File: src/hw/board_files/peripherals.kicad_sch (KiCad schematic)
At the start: 27 parts, among them J7 Conn_01x04, J8 Molex 104031-0811, Q1 PMOS, U5 NEO-M9N, U7 SHT30-DIS, U8 BQ27411DRZT-G1A

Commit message: Nearly done with layout
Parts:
- D6: footprint Package_TO_SOT_SMD:SOT-23-3 -> Package_TO_SOT_SMD:SOT-23_Handsoldering
- Q1: footprint Library:SOT91P240X110-3N_DMG2305UX-7 -> Package_TO_SOT_SMD:SOT-23_Handsoldering
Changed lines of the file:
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@@
 			)
 		)
-		(property "Footprint" "Package_TO_SOT_SMD:SOT-23-3"
+		(property "Footprint" "Package_TO_SOT_SMD:SOT-23_Handsoldering"
 			(at 233.68 73.66 0)
 			(effects
@@
 			)
 		)
-		(property "Footprint" "Library:SOT91P240X110-3N_DMG2305UX-7"
+		(property "Footprint" "Package_TO_SOT_SMD:SOT-23_Handsoldering"
 			(at 38.1 53.34 0)
 			(effects

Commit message: Updated BOM
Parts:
- R19: renamed from R22; footprint Resistor_SMD:R_0603_1608Metric_Pad0.98x0.95mm_HandSolder -> Resistor_SMD:R_1206_3216Metric_Pad1.30x1.75mm_HandSolder
- renumbered C18 to C17, C19 to C18, C20 to C19, C21 to C20, C22 to C21, D7 to D6, D6 to D7, J7 to J5, J8 to J6, R16 to R14, R17 to R15, R18 to R16, R19 to R17, R21 to R18, R24 to R20, R23 to R21, R20 to R22, TP10 to TP8, TP12 to TP9, U5 to U4, U7 to U5, U8 to U6
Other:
- note added: "Sense resistor (R19) 1% tolerance 1W rating"
- note removed: "Sense resistor (R22) 1% tolerance 1W rating"

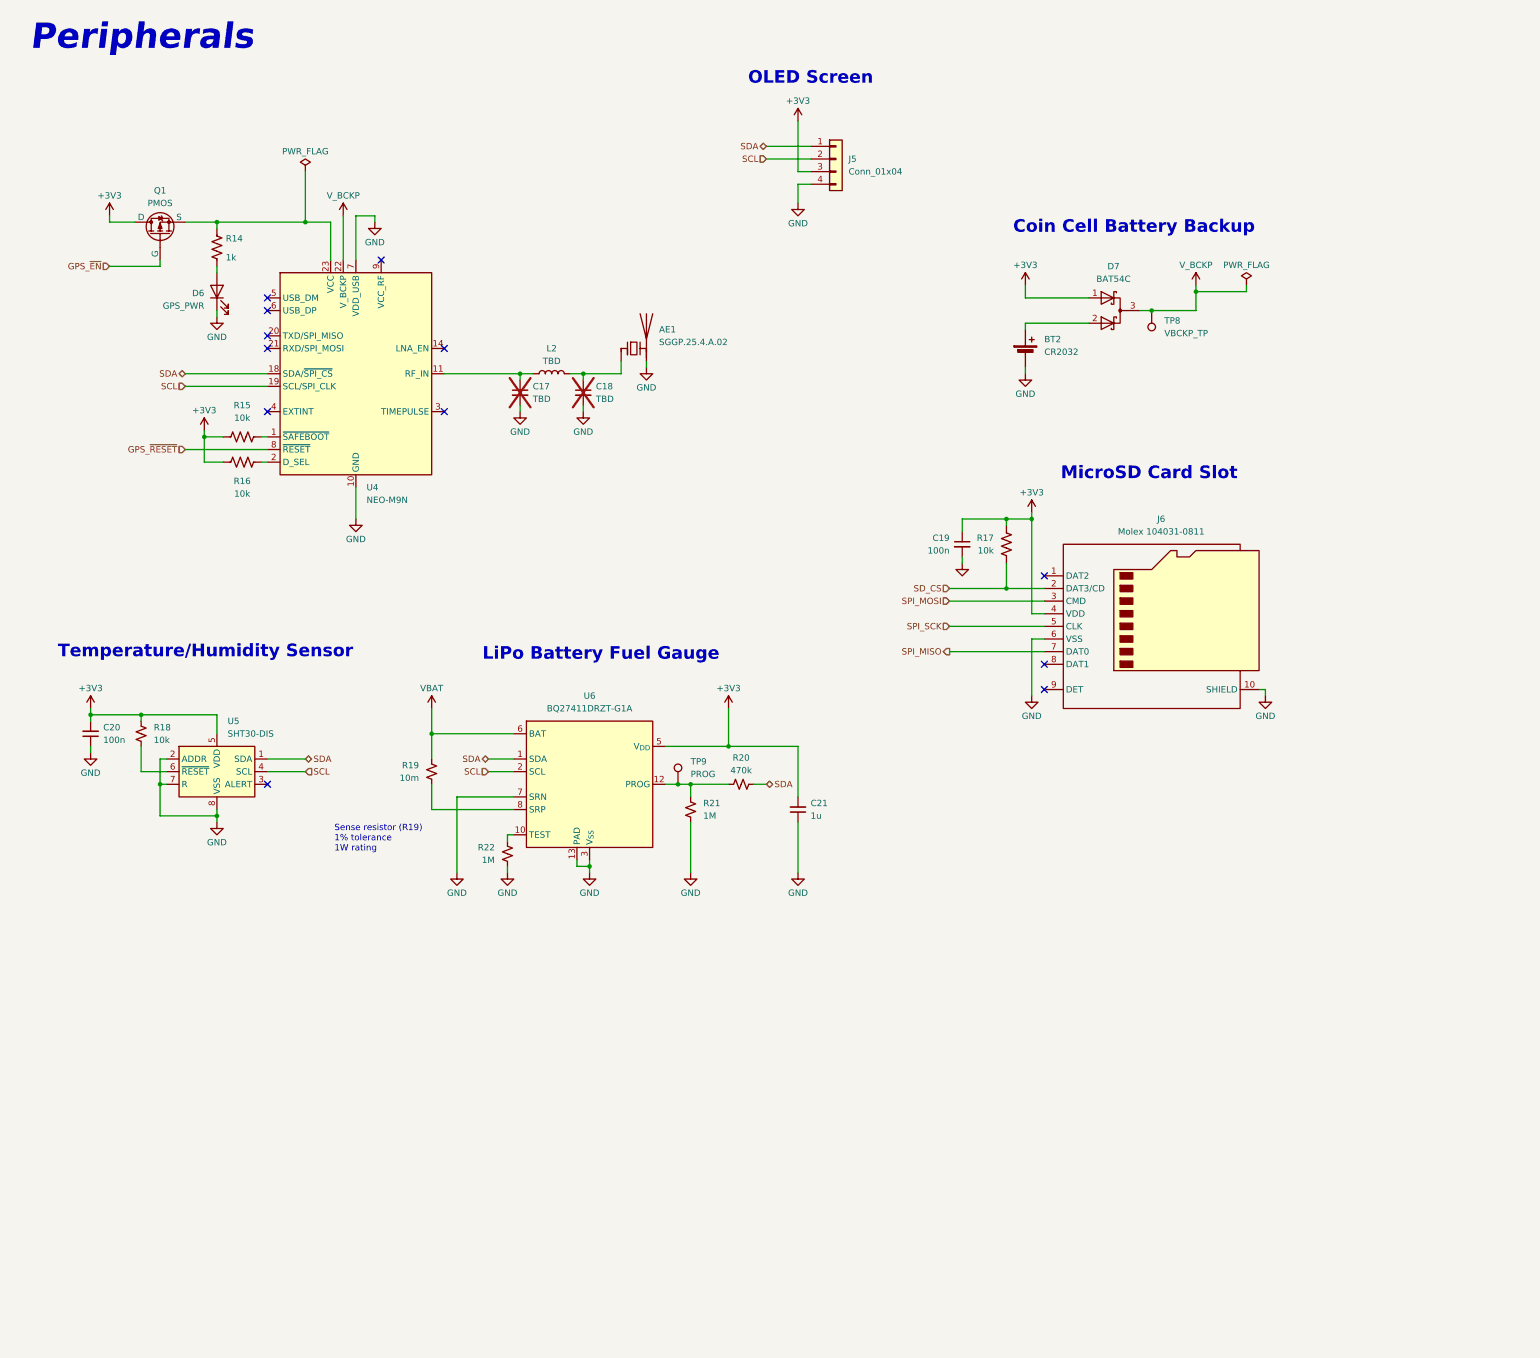
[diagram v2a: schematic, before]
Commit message: Schematic updates
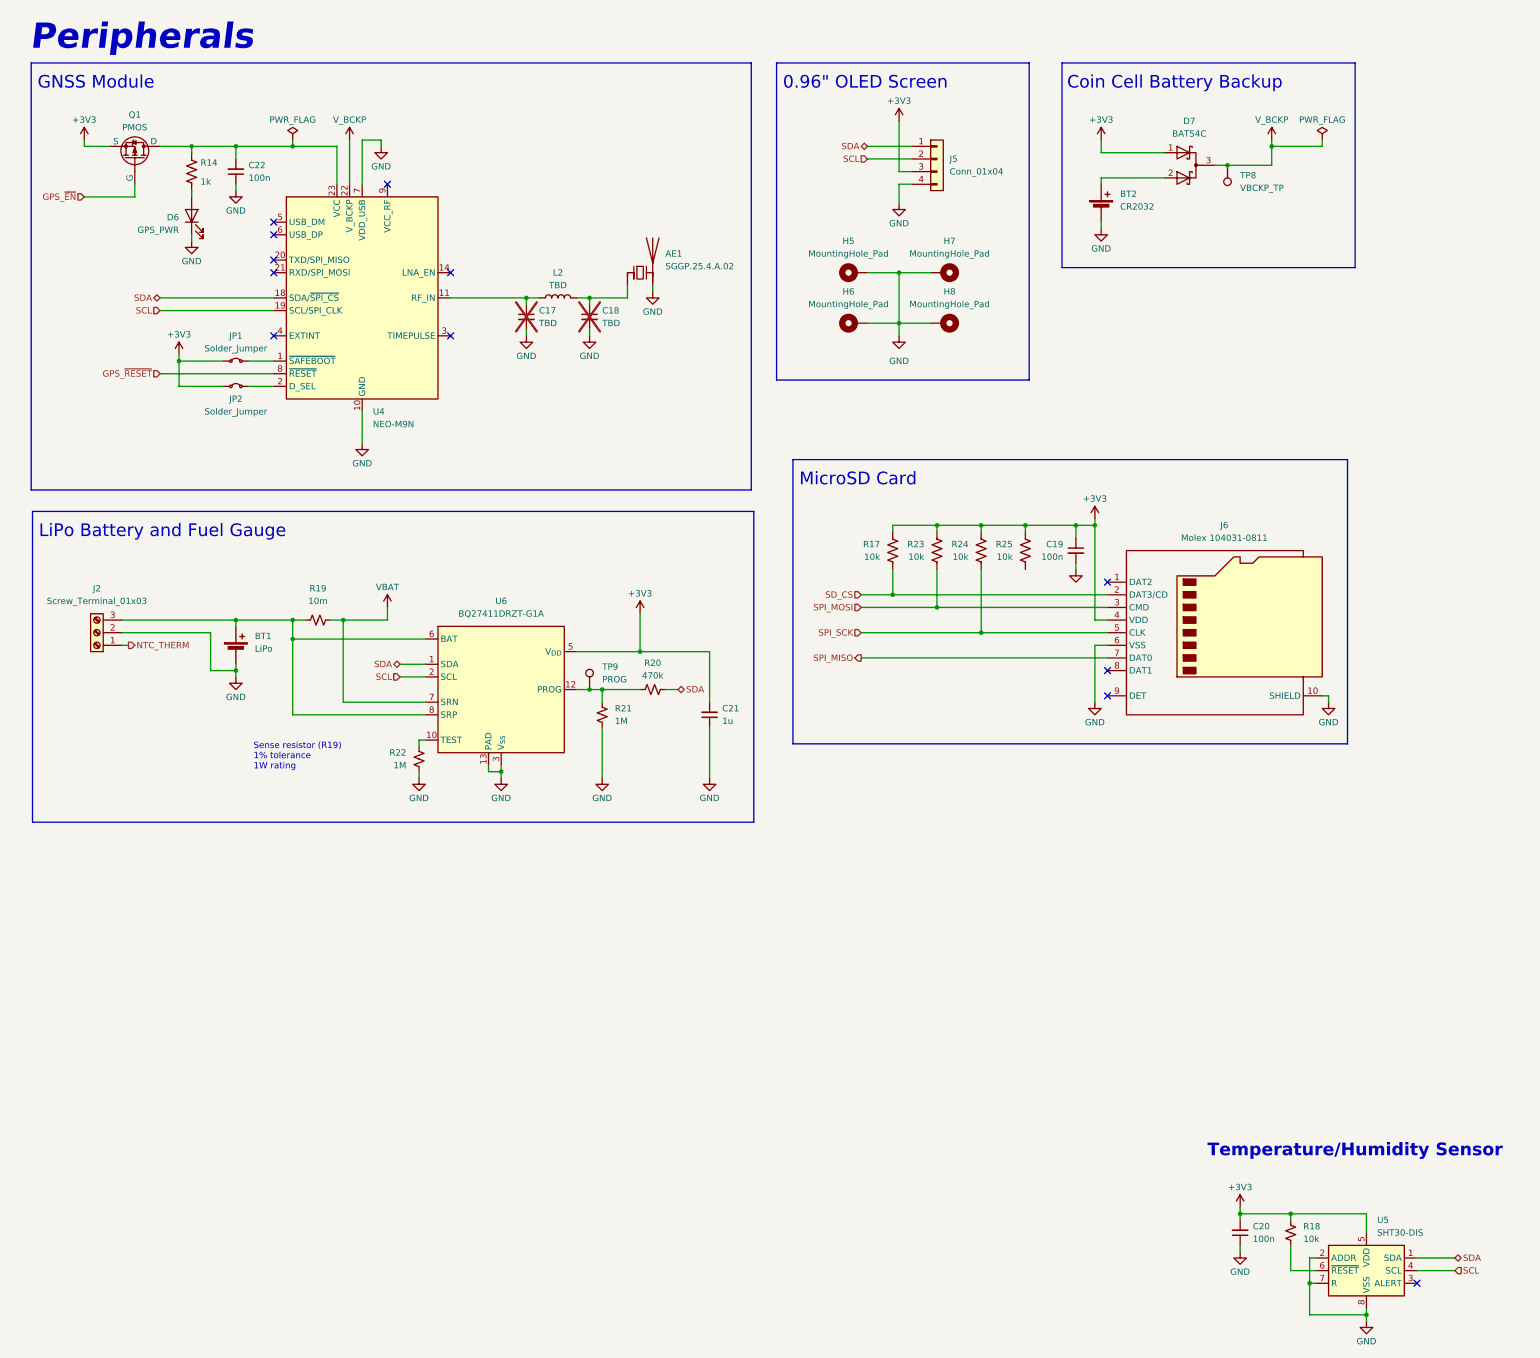
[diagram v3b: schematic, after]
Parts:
- removed R15, R16: 10k, Resistor_SMD:R_0603_1608Metric_Pad0.98x0.95mm_HandSolder, symbol Device:R_US
- added BT1: LiPo, Connector_JST:JST_PH_S2B-PH-K_1x02_P2.00mm_Horizontal, symbol Device:Battery_Cell
- added C22: 100n, Capacitor_SMD:C_0603_1608Metric_Pad1.08x0.95mm_HandSolder, symbol Device:C_Small
- added H5, H6, H7, H8: MountingHole_Pad, symbol Mechanical:MountingHole_Pad
- added J2: Screw_Terminal_01x03, TerminalBlock_Phoenix:TerminalBlock_Phoenix_MPT-0,5-3-2.54_1x03_P2.54mm_Horizontal, symbol Connector:Screw_Terminal_01x03
- added JP1, JP2: Solder_Jumper, Jumper:SolderJumper-2_P1.3mm_Open_TrianglePad1.0x1.5mm, symbol Jumper:Jumper_2_Small_Bridged
- added R23, R24, R25: 10k, Resistor_SMD:R_0603_1608Metric_Pad0.98x0.95mm_HandSolder, symbol Device:R_US
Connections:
- net +3V3: now also Q1.3 (S), JP1.1 (A), JP2.1 (A), R23.1, R24.1, R25.1; no longer Q1.1 (D)
- net GND: now also BT1.2 (-), C22.1, H5.1, H6.1, H7.1, H8.1, J2.2 (Pin_2); no longer U6.7 (SRN)
- net SPI_MOSI: now also R23.2
- net SPI_SCK: now also R24.2
- net VBAT: now also R19.2, U6.7 (SRN); no longer R19.1, U6.6 (BAT)
- net at U6.8 (SRP): now also R19.1, U6.6 (BAT), BT1.1 (+), J2.3 (Pin_3); no longer R19.2
- net at U4.1 (~{SAFEBOOT}): now also JP1.2 (B)
- net at U4.2 (D_SEL): now also JP2.2 (B)
- net at R14.1, U4.23 (VCC): now also Q1.1 (D), C22.2; no longer Q1.3 (S)
- new net NTC_THERM: J2.1 (Pin_1)
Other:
- note added: "0.96" OLED Screen"
- note added: "GNSS Module"
- note added: "LiPo Battery and Fuel Gauge"
- note added: "MicroSD Card"
- note removed: "LiPo Battery Fuel Gauge"
- note removed: "MicroSD Card Slot"
- note removed: "OLED Screen"
- moved on the sheet: AE1, BT2, C17, C18, C19, C20, C21, D6, D7, J5, J6, L2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

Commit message: Fixed fuel gauge IC schematic
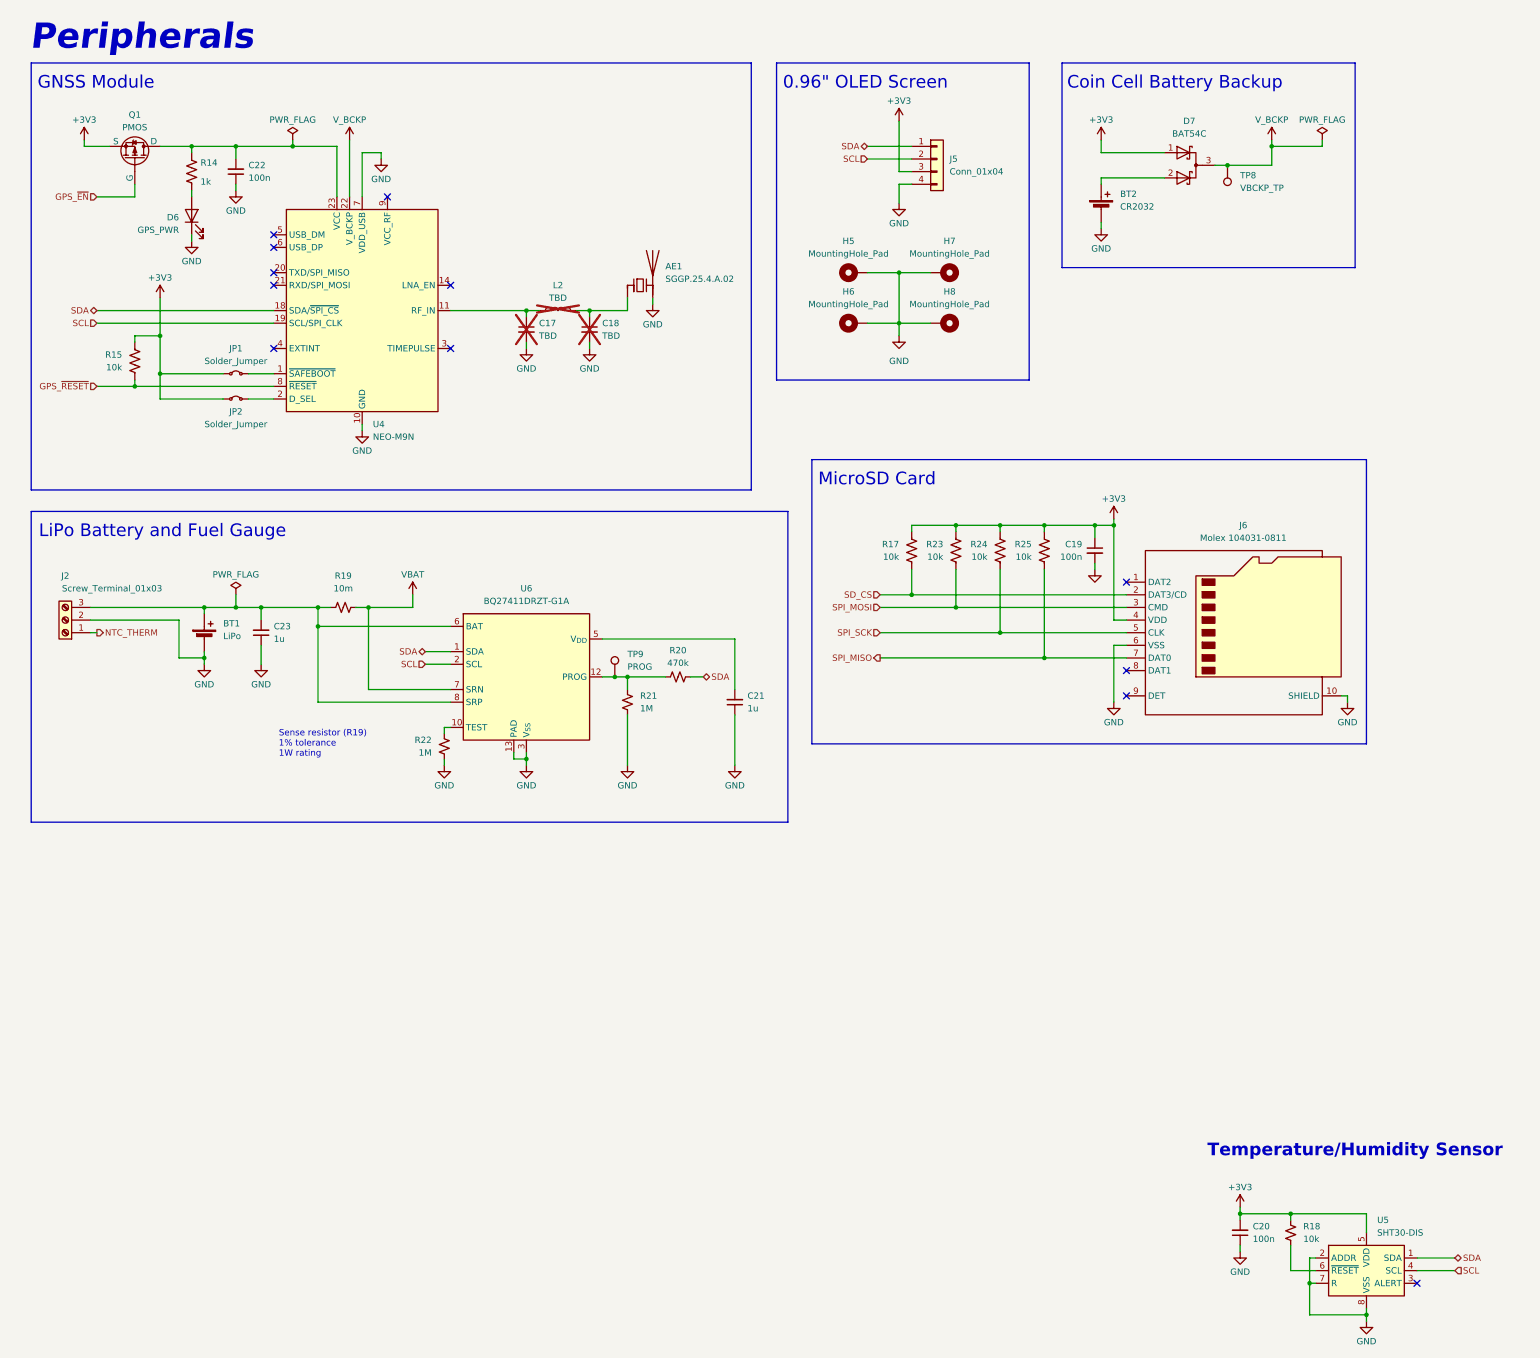
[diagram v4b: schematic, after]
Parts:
- added C23: 1u, Capacitor_SMD:C_0603_1608Metric_Pad1.08x0.95mm_HandSolder, symbol Device:C_Small
- added R15: 10k, Resistor_SMD:R_0603_1608Metric_Pad0.98x0.95mm_HandSolder, symbol Device:R_US
- L2: now not fitted; now left out of the parts list
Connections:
- net +3V3: now also R15.1; no longer C21.2, U6.5 (V_{DD})
- net GND: now also C23.1
- net GPS_~{RESET}: now also R15.2
- net SPI_MISO: now also R25.2
- net at BT1.1 (+), J2.3 (Pin_3), R19.1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: now also C23.2
- new net: C21.2, U6.5 (V_{DD})
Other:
- moved on the sheet: AE1, BT1, C17, C18, C19, C21, J2, J6, JP1, JP2, R17, R19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

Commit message: Added new OLED footprint. Finished schematic updates, started lyout. Changed 10 mOhm sense resistor PN to TCR of 50 ppm/C
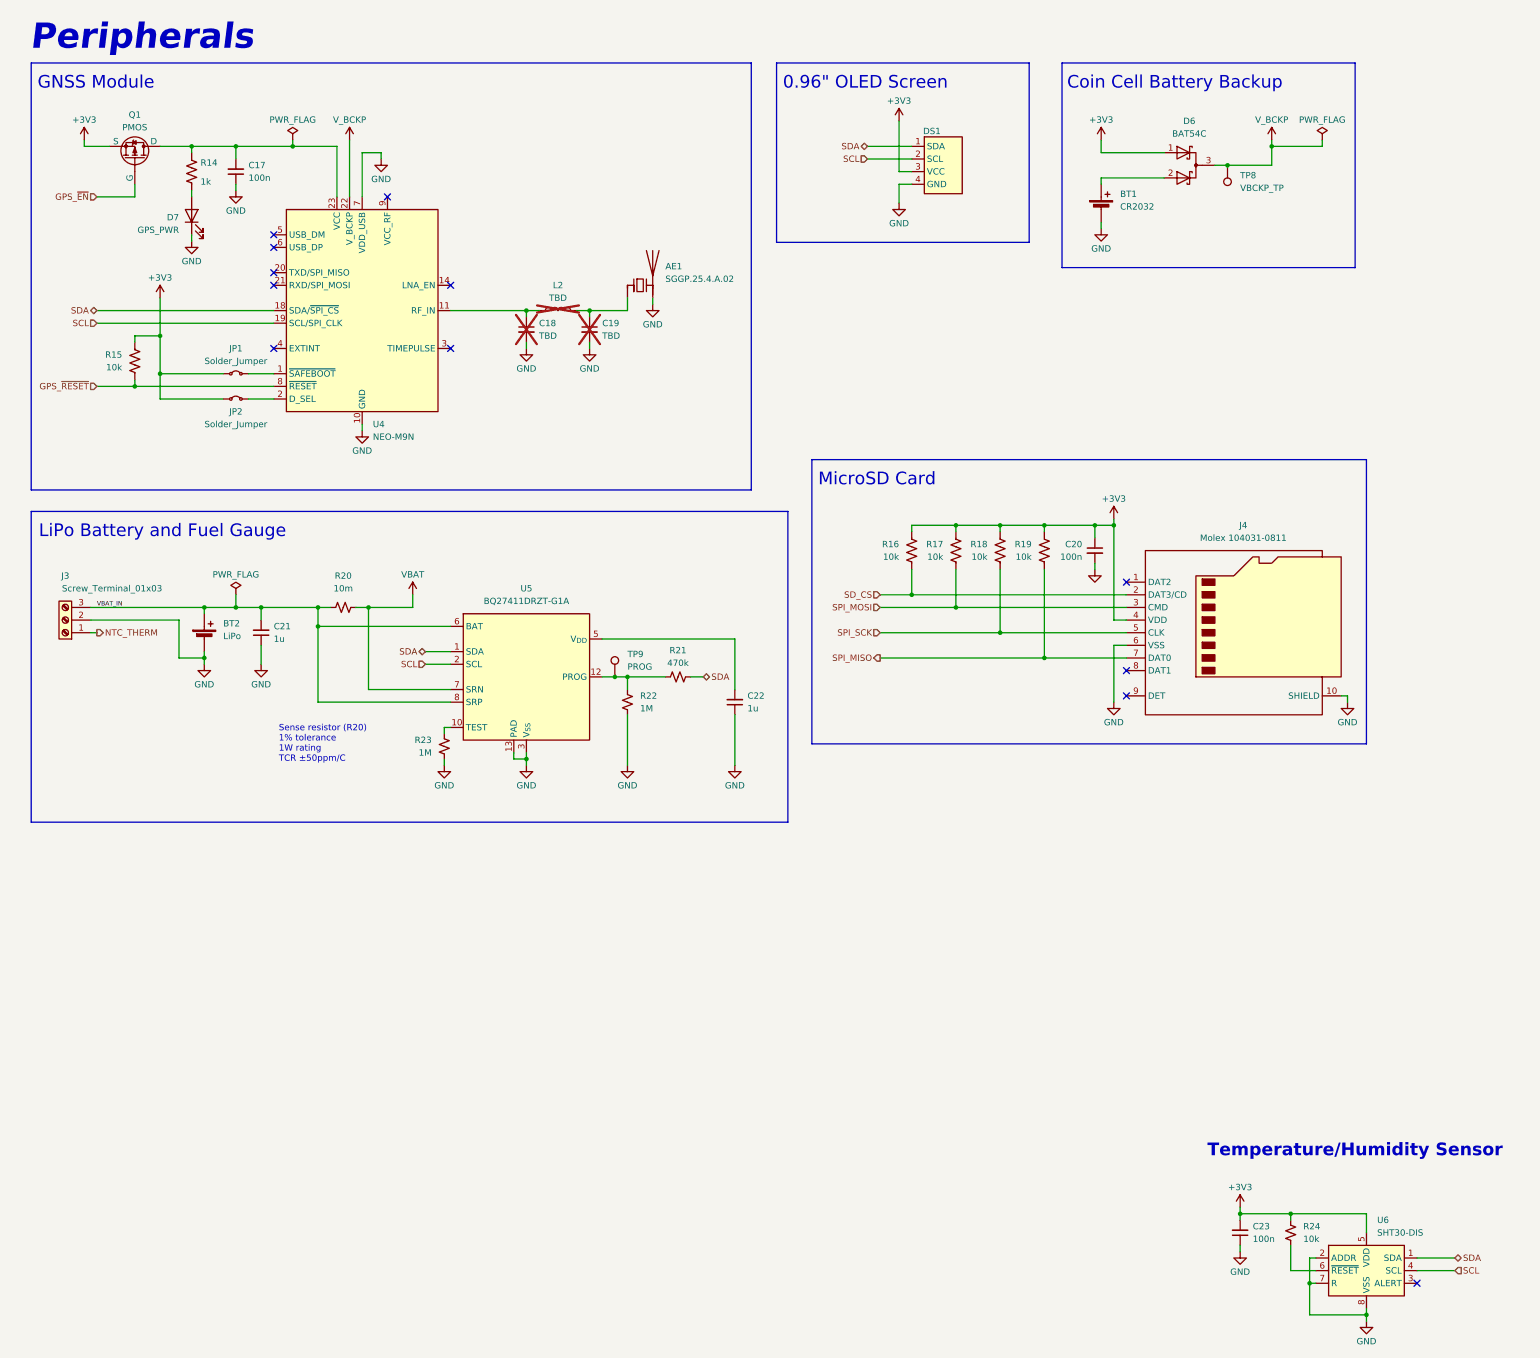
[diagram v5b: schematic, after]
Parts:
- removed H5, H6, H7, H8: MountingHole_Pad, symbol Mechanical:MountingHole_Pad
- removed J5: Conn_01x04, Connector_PinSocket_2.54mm:PinSocket_1x04_P2.54mm_Vertical, symbol Connector_Generic:Conn_01x04
- added DS1: ~, Project_Library:OLED_128x64_0.96in, symbol Project_Library:OLED_128x64
- J3: renamed from J2; footprint TerminalBlock_Phoenix:TerminalBlock_Phoenix_MPT-0,5-3-2.54_1x03_P2.54mm_Horizontal -> TerminalBlock_TE-Connectivity:TerminalBlock_TE_282834-3_1x03_P2.54mm_Horizontal
- renumbered BT2 to BT1, BT1 to BT2, C22 to C17, C17 to C18, C18 to C19, C19 to C20, C23 to C21, C21 to C22, C20 to C23, D7 to D6, D6 to D7, J6 to J4, R17 to R16, R23 to R17, R24 to R18, R25 to R19, R19 to R20, R20 to R21, R21 to R22, R22 to R23, R18 to R24, U6 to U5, U5 to U6
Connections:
- net +3V3: now also DS1.3 (VCC)
- net GND: now also DS1.4 (GND), DS1.5 (MOUNT)
- net SCL: now also DS1.2 (SCL)
- net SDA: now also DS1.1 (SDA)
- net VBAT_IN: now reaches BT2.1 (+), C21.2, J3.3 (Pin_3), R20.1, U5.6 (BAT), U5.8 (SRP)
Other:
- note added: "Sense resistor (R20) 1% tolerance 1W rating TCR ±50ppm/C"
- note removed: "Sense resistor (R19) 1% tolerance 1W rating"
